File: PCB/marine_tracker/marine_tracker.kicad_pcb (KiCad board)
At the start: 2 copper layers, 32 parts, among them J2 Conn_ARM_JTAG_SWD_10, SW1 SW_Push, U1 STM32U575RGT6, U2 SHT40, U3 AST50147-xx, U4 MIC5504-3.3YM5, U5 SAM-M10Q, U6 25CSM04T-I/SN, Y1 32kHz768, Y3 16MHz

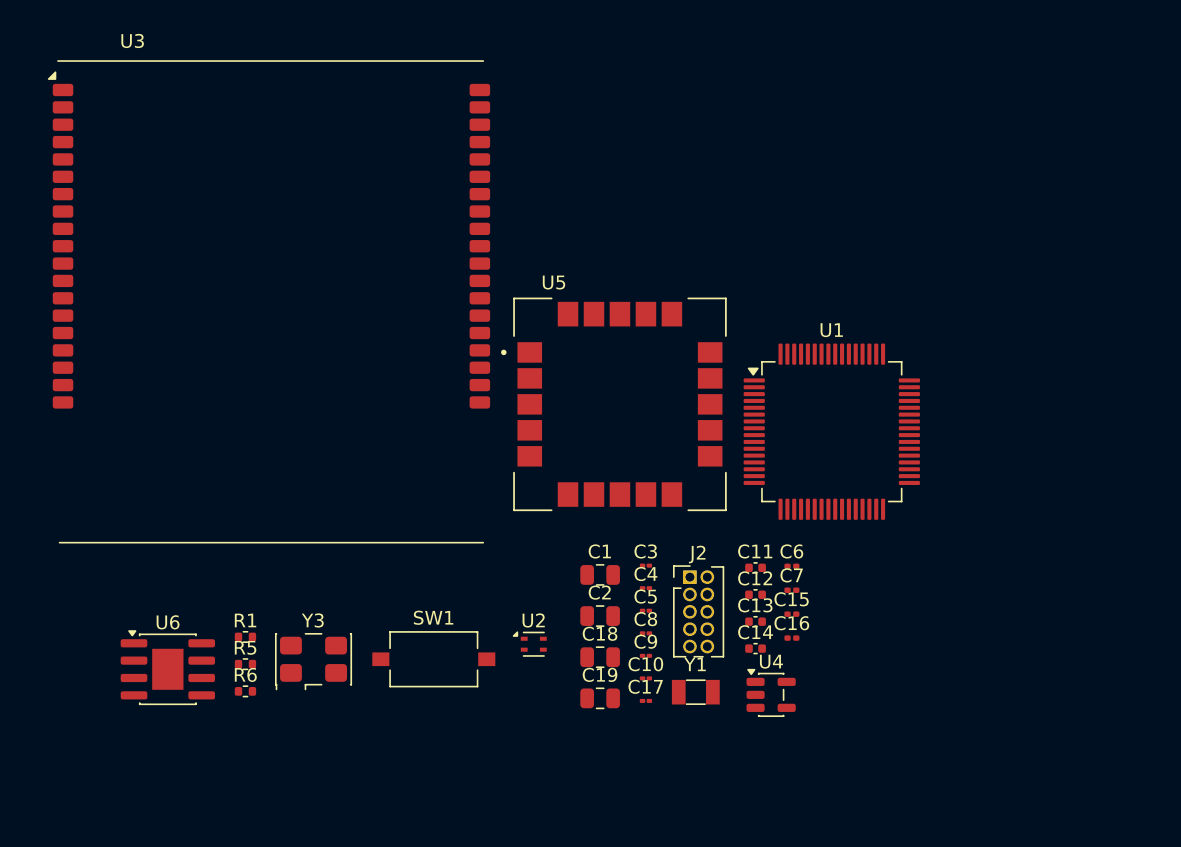
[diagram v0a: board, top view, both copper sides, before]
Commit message: add new connector for pressure sensor
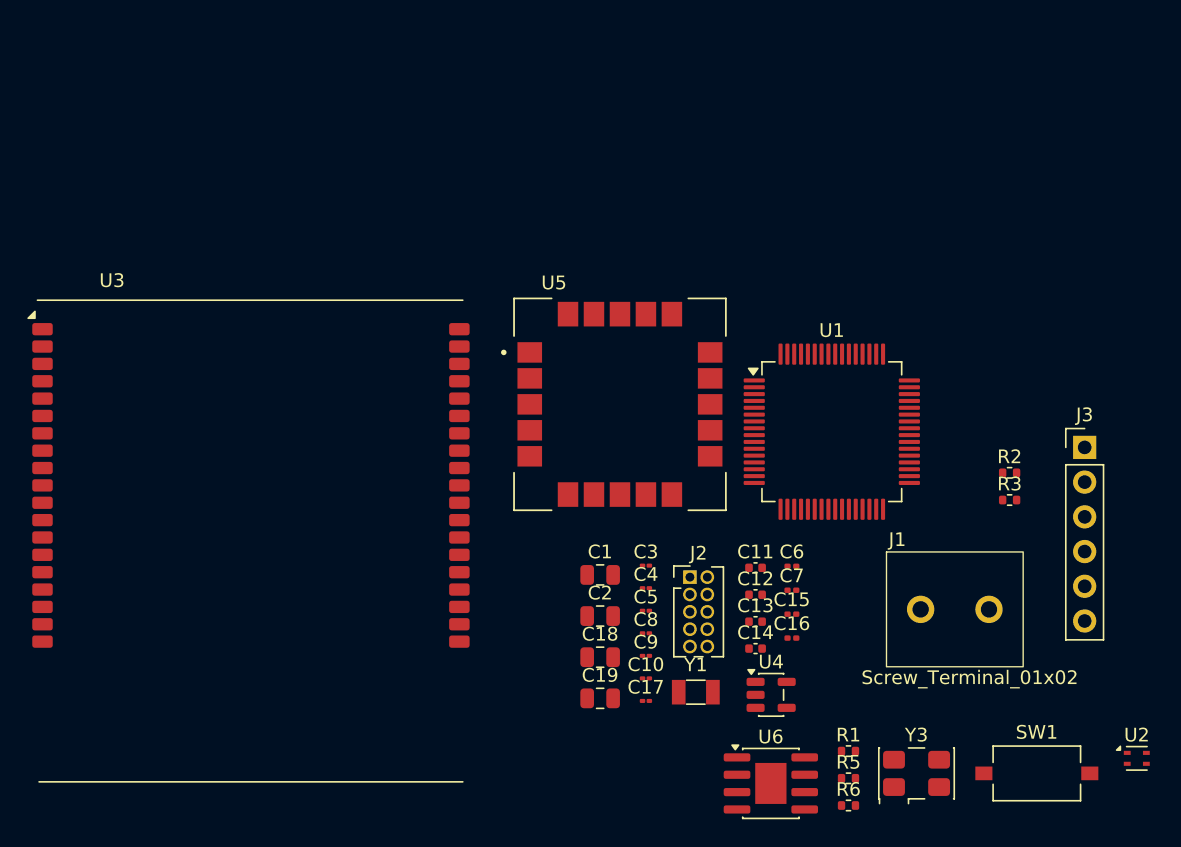
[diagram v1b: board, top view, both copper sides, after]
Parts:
- added J1: Screw_Terminal_01x02, Beuns_PCBFootprint:Screw_terminal_1x2, F.Cu at (92.5, 85.5)
- added J3: Conn_01x06_Pin, Connector_PinHeader_2.54mm:PinHeader_1x06_P2.54mm_Vertical, F.Cu at (104.5, 73.7)
- added R2: 10k, Resistor_SMD:R_0402_1005Metric, F.Cu at (99.0, 75.5)
- added R3: 10k, Resistor_SMD:R_0402_1005Metric, F.Cu at (99.0, 77.5)
- moved R1 44.9 mm to (87.2, 95.9)
- moved U2 44.9 mm to (108.3, 96.4)
- moved U6 44.9 mm to (81.5, 98.2)
- moved Y3 44.9 mm to (92.2, 97.5)
- moved R5 44.9 mm to (87.2, 97.9)
- moved R6 44.9 mm to (87.2, 99.8)
- moved SW1 44.9 mm to (101.0, 97.5)
- moved U3 17.6 mm to (43.5, 80.5)
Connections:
- U1 pad 10: unconnected-(U1-PC2-Pad10) -> PRE_SPI2_MISO
- U1 pad 29: unconnected-(U1-PB10-Pad29) -> PRE_SPI2_SCK
- U1 pad 34: unconnected-(U1-PB13-Pad34) -> PRES_I2C2_SCL
- U1 pad 35: unconnected-(U1-PB14-Pad35) -> PRES_I2C2_SDA
- U1 pad 9: unconnected-(U1-PC1-Pad9) -> PRE_SPI2_MOSI

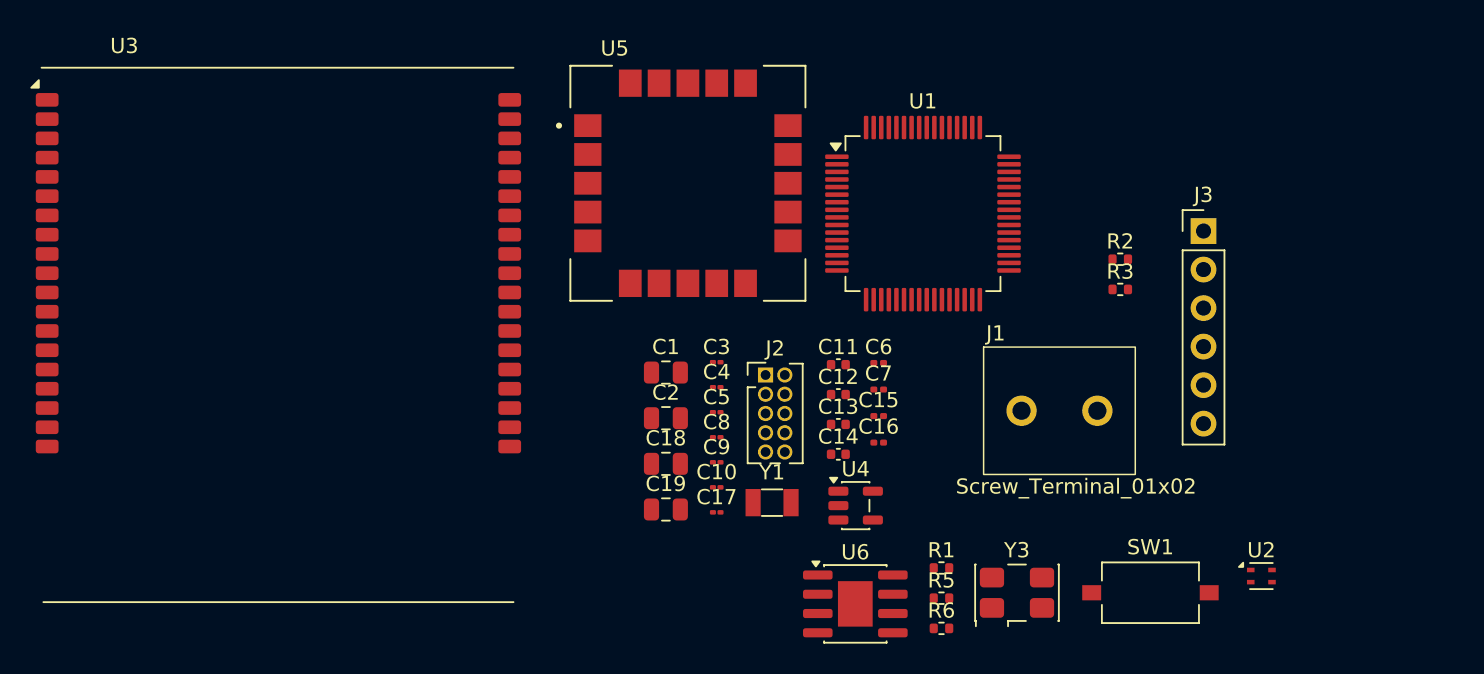
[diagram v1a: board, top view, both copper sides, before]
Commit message: add connector for satellite communication module
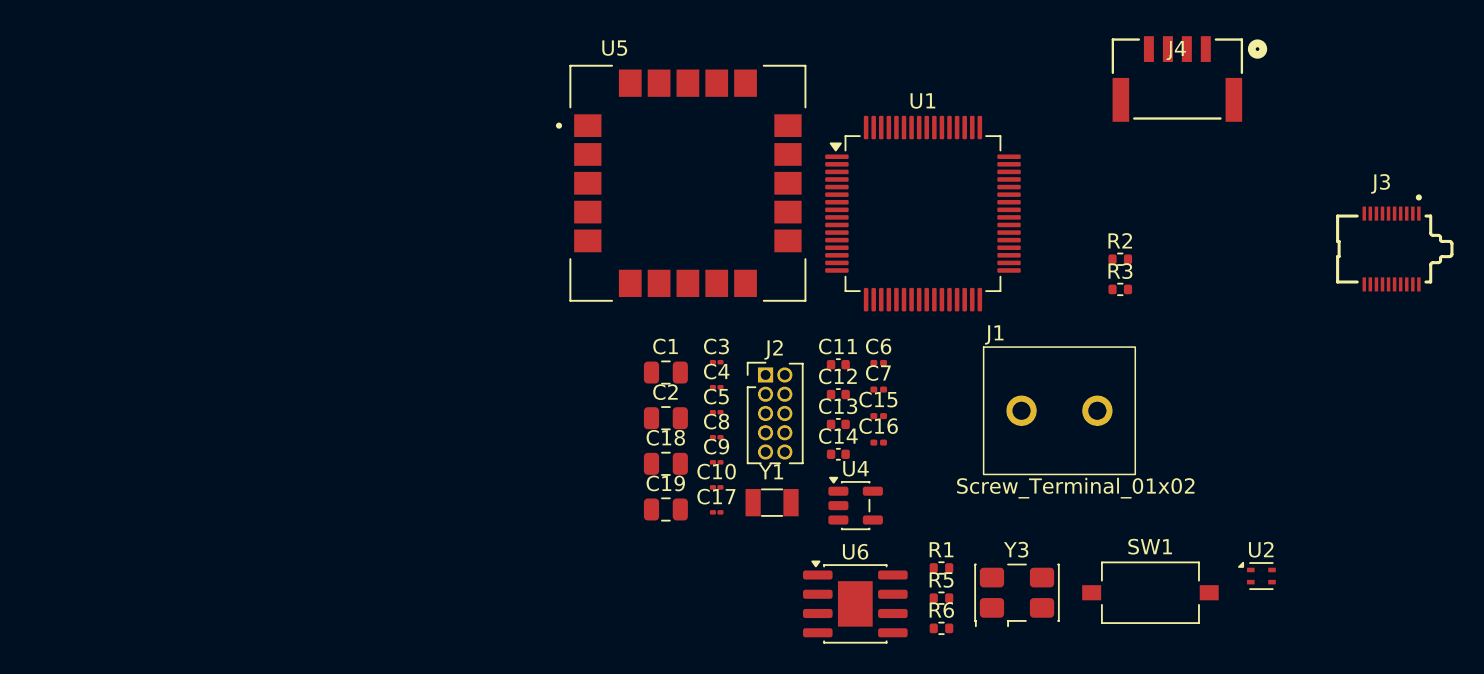
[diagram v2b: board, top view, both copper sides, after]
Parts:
- removed U3: AST50147-xx, RF_Module:Astrocast_AST50147-00
- added J4: BM04B-GHS-TBT, Beuns_PCBFootprint:CONN_BM04B-GHS-TBT_JST, F.Cu at (102.8, 63.6)
- J3: value Conn_01x06_Pin -> SS4-10-3.00-L-D-K-TR; footprint Connector_PinHeader_2.54mm:PinHeader_1x06_P2.54mm_Vertical -> Beuns_PCBFootprint:SAMTEC_SS4-10-3.00-L-D-TR
- moved J3 12.5 mm to (116.9, 74.8)
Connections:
- U1 pad 10: PRE_SPI2_MISO -> unconnected-(U1-PC2-Pad10)
- U1 pad 29: PRE_SPI2_SCK -> unconnected-(U1-PB10-Pad29)
- U1 pad 9: PRE_SPI2_MOSI -> unconnected-(U1-PC1-Pad9)

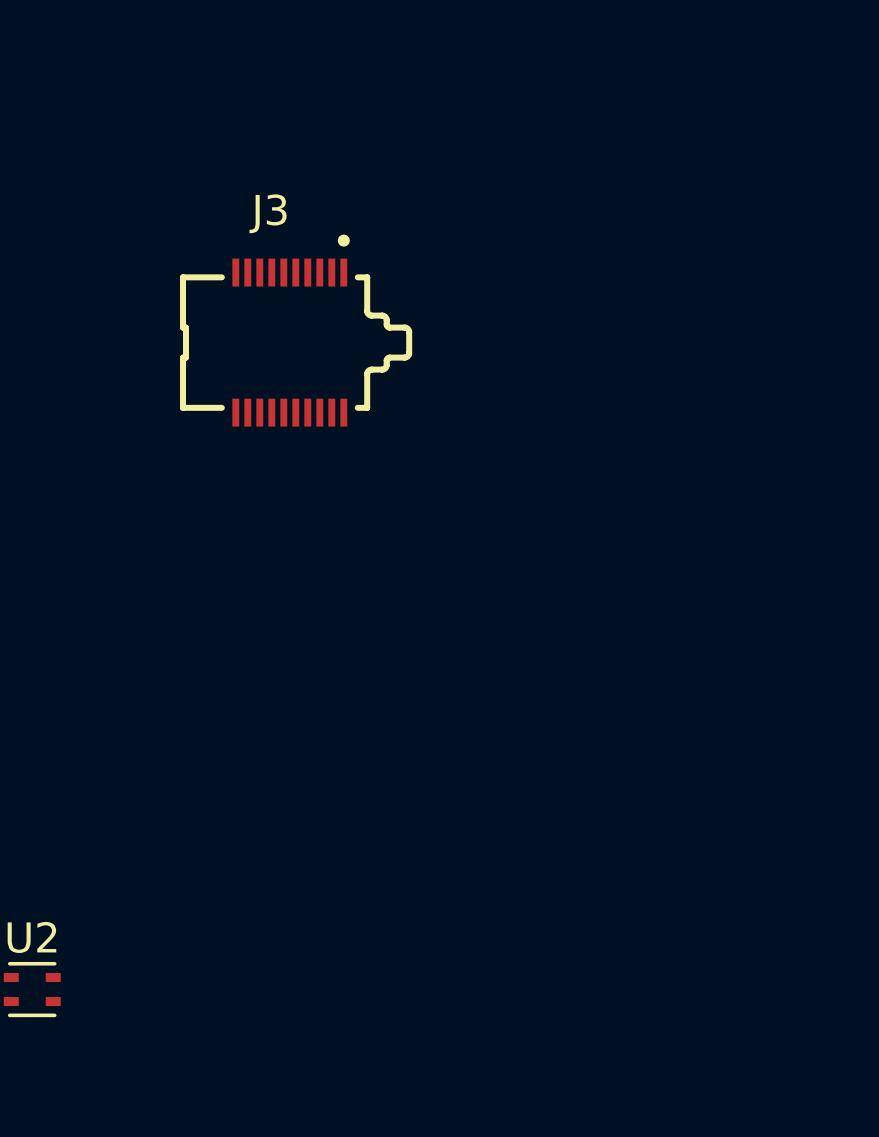
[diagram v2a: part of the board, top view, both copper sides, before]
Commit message: add 3D models
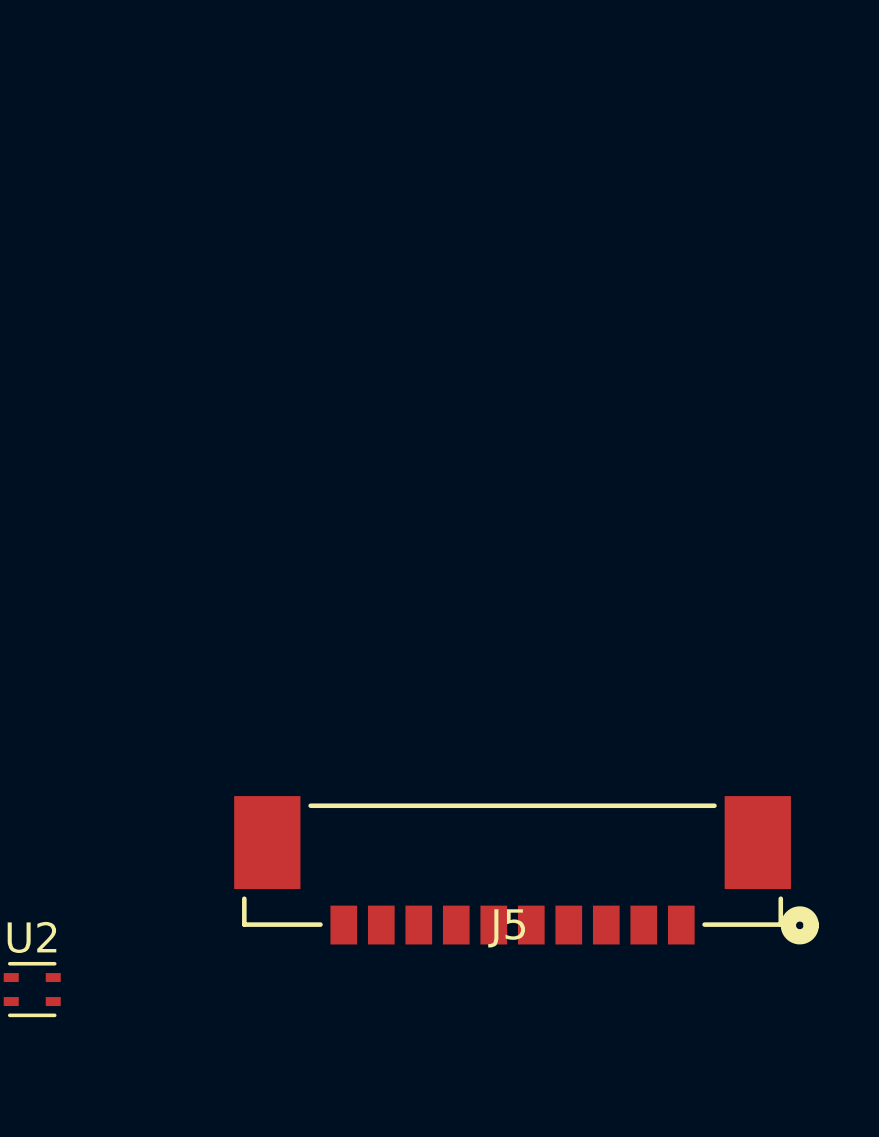
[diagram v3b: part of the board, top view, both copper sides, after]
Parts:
- removed J3: SS4-10-3.00-L-D-K-TR, Beuns_PCBFootprint:SAMTEC_SS4-10-3.00-L-D-TR
- added J5: molex_533981071, Beuns_PCBFootprint:CONN10_533981071_MOL, F.Cu at (124.3, 92.3)
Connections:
- U1 pad 16: AST_RXD -> SAT_RXD
- U1 pad 17: AST_TXD -> SAT_TXD
- U1 pad 20: AST_WAKEUP -> SAT_CTS
- U1 pad 21: AST_RST -> SAT_RTS
- U1 pad 22: AST_EVENT -> SAT_NetAv
- U1 pad 23: AST_ANTUSE -> SAT_RI
- U1 pad 41: unconnected-(U1-PA8-Pad41) -> SAT_OnOff

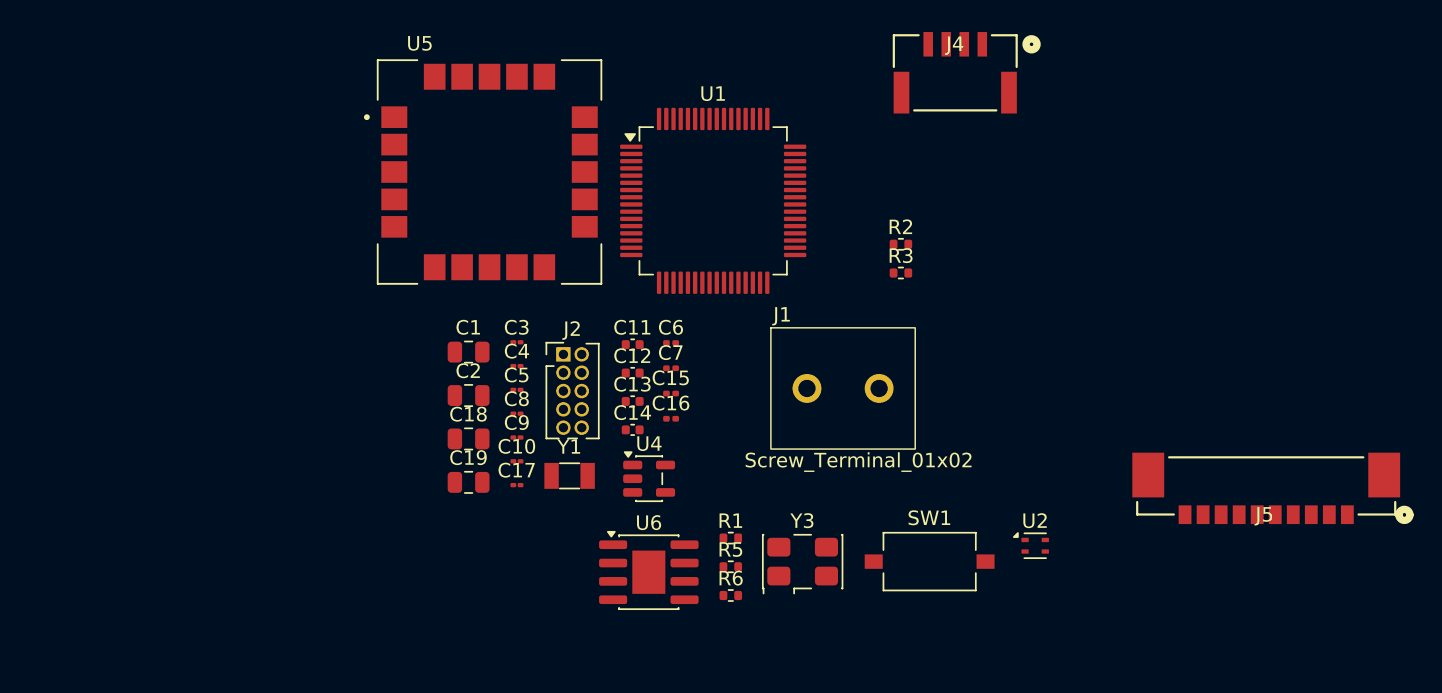
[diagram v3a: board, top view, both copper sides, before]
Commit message: Component Placement + export Step file PCB
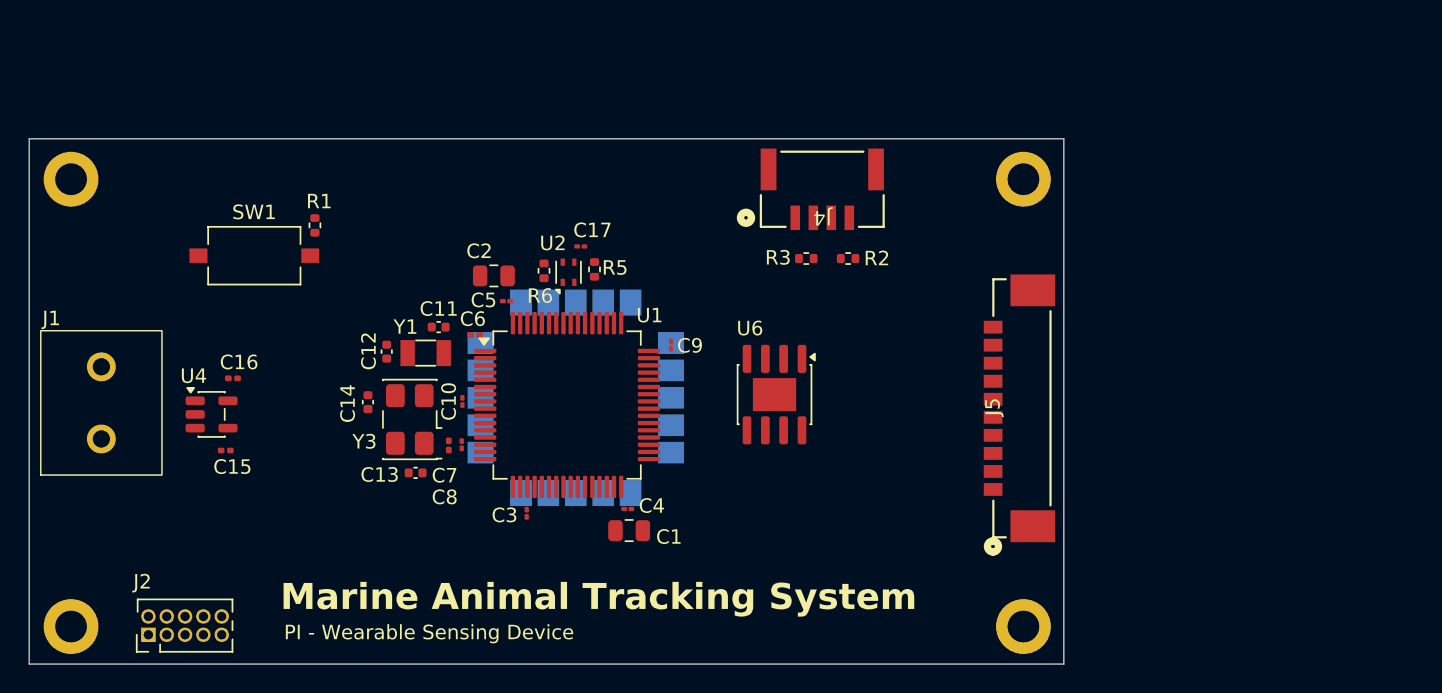
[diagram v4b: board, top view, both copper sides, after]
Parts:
- removed C18, C19: 10u, Capacitor_SMD:C_0805_2012Metric
- added REF**: MountingHole_2.2mm_M2_DIN965_Pad, MountingHole:MountingHole_2.2mm_M2_DIN965_Pad, F.Cu at (107.5, 71.0)
- added REF**: MountingHole_2.2mm_M2_DIN965_Pad, MountingHole:MountingHole_2.2mm_M2_DIN965_Pad, F.Cu at (107.5, 102.0)
- added REF**: MountingHole_2.2mm_M2_DIN965_Pad, MountingHole:MountingHole_2.2mm_M2_DIN965_Pad, F.Cu at (41.5, 102.0)
- added REF**: MountingHole_2.2mm_M2_DIN965_Pad, MountingHole:MountingHole_2.2mm_M2_DIN965_Pad, F.Cu at (41.5, 71.0)
- U5: moved to B.Cu
- moved SW1 51.4 mm to (54.2, 76.3)
- moved J1 49.0 mm to (43.6, 89.0), turned to 90 degrees
- moved U2 37.5 mm to (76.0, 77.5), turned to 90 degrees
- moved R1 36.1 mm to (58.4, 74.2), turned to 90 degrees
- moved J2 34.7 mm to (46.9, 102.6), turned to 90 degrees
- moved C15 31.1 mm to (52.2, 89.8)
- moved U4 30.6 mm to (51.2, 87.3)
- moved C16 30.5 mm to (52.7, 84.8)
- moved Y3 29.0 mm to (65.0, 87.7), turned to 90 degrees
- moved R6 26.0 mm to (74.3, 77.3), turned to -90 degrees
- moved R5 22.7 mm to (77.8, 77.2), turned to -90 degrees
- moved C14 18.4 mm to (62.1, 86.5), turned to 90 degrees
- moved J5 17.8 mm to (107.4, 86.9), turned to -90 degrees
- moved U1 17.4 mm to (75.9, 86.7)
- moved C17 17.1 mm to (76.8, 75.7)
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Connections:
- Y3 pad 2: (no net) -> GND
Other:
- board outline added: 71.7 x 36.4 mm
- board text added: "Marine Animal Tracking System"
- board text added: "PI - Wearable Sensing Device"
